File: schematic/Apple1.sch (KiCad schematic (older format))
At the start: 62 parts, among them J1 RCJ-041, J2 USB_A, J4 PWR, J5 ARM_JTAG_SWD, J6 SLOT, J7 EDGE, J8 12V, J9 -12V, SW1 RST, SW2 CLEAR, SW3 PWR, U1 WD65C02, U10 L7805, U2 6821 (W65C21N), U3 ATSAMD21E18A-A, U4 74LS138, U5 AT28C64B-15PU, U6 AS6C62256, U7 74HC00, U9 LD33CV

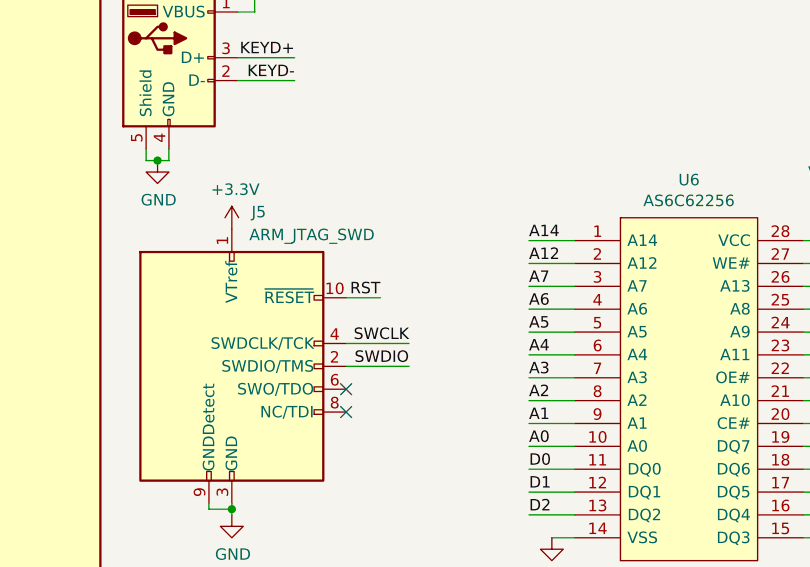
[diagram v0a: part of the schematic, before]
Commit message: final here, attempting to move to compute module to use modern display (HDMI)
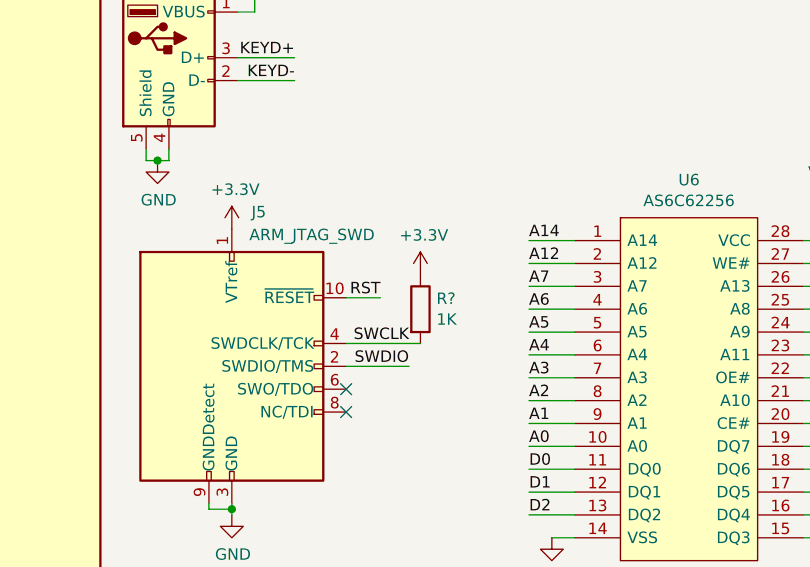
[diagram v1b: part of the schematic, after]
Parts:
- added R?: 1K, symbol Device:R
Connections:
- net +3V3: now also R?.1
- net SWCLK: now also R?.2
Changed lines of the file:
@@
 Text Label 4050 6050 2    50   ~ 0
 SWCLK
-Wire Wire Line
-	4050 6050 3775 6050
 $Comp
 L power:+3.3V #PWR0136
@@
 Wire Wire Line
 	3000 5200 3000 5250
-$Comp
-L Connector:USB_A J2
-U 1 1 5F306103
-P 3000 4800
-F 0 "J2" H 3057 5267 50  0000 C CNN
-F 1 "USB_A" H 3057 5176 50  0000 C CNN
-F 2 "UJ2-AH-4-TH:CUI_UJ2-AH-4-TH" H 3150 4750 50  0001 C CNN
-F 3 " ~" H 3150 4750 50  0001 C CNN
-	1    3000 4800
-	1    0    0    -1
-$EndComp
 Connection ~ 2950 5250
 Wire Wire Line
@@
 Wire Wire Line
 	4650 1025 5375 1025
+$Comp
+L Connector:USB_A J2
+U 1 1 5FAEFE8A
+P 3000 4800
+F 0 "J2" H 3057 5267 50  0000 C CNN
+F 1 "USB_A" H 3057 5176 50  0000 C CNN
+F 2 "UJ2-AH-4-TH:CUI_UJ2-AH-4-TH" H 3150 4750 50  0001 C CNN
+F 3 " ~" H 3150 4750 50  0001 C CNN
+	1    3000 4800
+	1    0    0    -1
+$EndComp
+$Comp
+L Device:R R?
+U 1 1 5FCC40B0
+P 4100 5900
+F 0 "R?" H 4170 5946 50  0000 L CNN
+F 1 "1K" H 4170 5855 50  0000 L CNN
+F 2 "" V 4030 5900 50  0001 C CNN
+F 3 "~" H 4100 5900 50  0001 C CNN
+	1    4100 5900
+	1    0    0    -1
+$EndComp
+Wire Wire Line
+	3775 6050 4100 6050
+$Comp
+L power:+3.3V #PWR?
+U 1 1 5FD027A3
+P 4100 5750
+F 0 "#PWR?" H 4100 5600 50  0001 C CNN
+F 1 "+3.3V" H 4115 5923 50  0000 C CNN
+F 2 "" H 4100 5750 50  0001 C CNN
+F 3 "" H 4100 5750 50  0001 C CNN
+	1    4100 5750
+	1    0    0    -1
+$EndComp
 $EndSCHEMATC

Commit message: rpi final
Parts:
- removed C11: 10uF, Capacitor_THT:CP_Radial_D5.0mm_P2.50mm, symbol Device:CP1_Small
- removed C17: 1uF, Capacitor_THT:CP_Radial_D5.0mm_P2.50mm, symbol Device:C_Small
- removed C8, C9: 0.1uF, Capacitor_THT:C_Rect_L7.0mm_W2.5mm_P5.00mm, symbol Device:C_Small
- removed J1: RCJ-041, CUI_RCJ-041, symbol RCJ-041:RCJ-041
- removed J2: USB_A, UJ2-AH-4-TH:CUI_UJ2-AH-4-TH, symbol Connector:USB_A
- removed J5: ARM_JTAG_SWD, Connector_PinSocket_1.27mm:PinSocket_2x05_P1.27mm_Vertical, symbol Connector:Conn_ARM_JTAG_SWD_10
- removed R10, R11, R12, R13, R14, R25, R6, R7, R8, R9: 1K, Resistor_THT:R_Axial_DIN0207_L6.3mm_D2.5mm_P7.62mm_Horizontal, symbol Device:R_Small
- removed R15, R16, R17, R18, R20, R21, R22, R23, R24: 2k, Resistor_THT:R_Axial_DIN0207_L6.3mm_D2.5mm_P7.62mm_Horizontal, symbol Device:R_Small
- removed R26: 560, Resistor_THT:R_Axial_DIN0207_L6.3mm_D2.5mm_P7.62mm_Horizontal, symbol Device:R_Small
- removed R27: 220, Resistor_THT:R_Axial_DIN0207_L6.3mm_D2.5mm_P7.62mm_Horizontal, symbol Device:R_Small
- removed R5: 3.3K, Resistor_THT:R_Axial_DIN0207_L6.3mm_D2.5mm_P7.62mm_Horizontal, symbol Device:R
- removed R?: 1K, symbol Device:R
- removed SW2: CLEAR, Button_Switch_THT:SW_PUSH_6mm, symbol Switch:SW_SPST
- removed U3: ATSAMD21E18A-A, Package_QFP:TQFP-32_7x7mm_P0.8mm, symbol SAMD:ATSAMD21E18A-A
- removed U9: LD33CV, Package_TO_SOT_THT:TO-220-3_Vertical, symbol Regulator_Linear:LD1117S33TR_SOT223
- added C11, C12, C19, C20: 10uF, Capacitor_SMD:C_0603_1608Metric_Pad1.08x0.95mm_HandSolder, symbol Device:C_Small
- added C2: 0.1uF, Capacitor_SMD:C_0603_1608Metric_Pad1.08x0.95mm_HandSolder, symbol Device:C_Small
- added C21, C22: 0.47uF, Capacitor_SMD:C_0603_1608Metric_Pad1.08x0.95mm_HandSolder, symbol Device:C_Small
- added L1, L2: 4.7uH, Inductor_SMD:L_Bourns-SRN4018, symbol Device:L_Small
- added R19: 100k, Resistor_SMD:R_0603_1608Metric, symbol Device:R_Small
- added U12: AP7315DQ-2.5, Package_TO_SOT_SMD:SOT-23-5, symbol Regulator_Linear:AP7315DQ-25W5-7
- added U5: PAM2306AYPKE, Package_DFN_QFN:WDFN-12-1EP_3x3mm_P0.45mm_EP1.7x2.5mm, symbol Regulator_Switching:PAM2306AYPKE
- C1: renamed from C10; value 10uF -> 0.33uF; footprint Capacitor_THT:CP_Radial_D5.0mm_P2.50mm -> Capacitor_SMD:C_0603_1608Metric_Pad1.08x0.95mm_HandSolder
- C3: renamed from C12; value 1uF -> 0.1uF; footprint Capacitor_THT:CP_Radial_D5.0mm_P2.50mm -> Capacitor_SMD:C_0603_1608Metric_Pad1.08x0.95mm_HandSolder
- renumbered C7 to C10, C1 to C4, C2 to C5, C3 to C6, C4 to C7, C5 to C8, C6 to C9, J4 to J1, J7 to J2, J6 to J3, J8 to J4, J9 to J5, R19 to R5, SW3 to SW1, SW1 to SW2, U4 to U1, U6 to U2, U1 to U3, U7 to U4, U2 to U6, U10 to U7, U5 to U8
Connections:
- net +3V3: now also C20.1, C21.1, L1.2, U12.1 (VIN), U12.3 (EN), U5.4 (FB1)
- net GND: now also C11.2, C12.2, C19.2, C2.1, C20.2, C21.2, C22.2, U12.2 (GND), U5.13 (GND), U5.3 (GND), U5.9 (GND)
- net VCC renamed +5V
- net +5V: now also C11.1, C12.1, R19.1, U5.1 (VIN2), U5.6 (EN1), U5.7 (VIN1)
- new net: C2.2, R19.2, U5.12 (EN2)
- new net: L2.1, U5.2 (LX2)
- new net: L1.1, U5.8 (LX1)
- new net +1V8: C19.1, L2.2, U5.10 (FB2)
- new net +2V5: C22.1, U12.5 (VOUT)
- no-connect marks 10 -> 8
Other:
- moved on the sheet: C1, C3, D1, J1, R1, R2, R3, R4, SW1, SW2, U1, U2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

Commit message: completed schematic
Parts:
- renumbered C4 to C10, C5 to C11, C6 to C12, C7 to C13, C8 to C14, C9 to C15, C10 to C16, C3 to C2, C2 to C3, C11 to C4, C12 to C5, C19 to C6, C20 to C7, C21 to C8, C22 to C9, R19 to R4, R4 to R5, R5 to R6, U3 to U1, U12 to U10, U6 to U2, U2 to U3, U8 to U4, U1 to U5, U5 to U8, U4 to U9

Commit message: finished product v1
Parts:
- removed C3: 0.1uF, Capacitor_SMD:C_0603_1608Metric_Pad1.08x0.95mm_HandSolder, symbol Device:C_Small
- removed C4, C5, C6, C7: 10uF, Capacitor_SMD:C_0603_1608Metric_Pad1.08x0.95mm_HandSolder, symbol Device:C_Small
- removed C8, C9: 0.47uF, Capacitor_SMD:C_0603_1608Metric_Pad1.08x0.95mm_HandSolder, symbol Device:C_Small
- removed L1, L2: 4.7uH, Inductor_SMD:L_Bourns-SRN4018, symbol Device:L_Small
- removed R4: 100k, Resistor_SMD:R_0603_1608Metric, symbol Device:R_Small
- removed U10: AP7315DQ-2.5, Package_TO_SOT_SMD:SOT-23-5, symbol Regulator_Linear:AP7315DQ-25W5-7
- removed U8: PAM2306AYPKE, Package_DFN_QFN:WDFN-12-1EP_3x3mm_P0.45mm_EP1.7x2.5mm, symbol Regulator_Switching:PAM2306AYPKE
- J1: symbol Connector:Barrel_Jack_Switch -> Apple1-rescue:Barrel_Jack_Switch-Connector
- J4, J5: symbol Connector:Conn_01x01_Male -> Apple1-rescue:Conn_01x01_Male-Connector
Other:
- moved on the sheet: D2, R6

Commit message: finished apple 1
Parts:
- C1, C2: footprint Capacitor_SMD:C_0603_1608Metric_Pad1.08x0.95mm_HandSolder -> Capacitor_THT:C_Rect_L7.0mm_W2.5mm_P5.00mm
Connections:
- net GND: no longer J3.MH1, J3.MH2
- no-connect marks 8 -> 10
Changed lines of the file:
@@
 F 0 "C1" H 2325 1025 50  0000 L CNN
 F 1 "0.33uF" H 2300 925 50  0000 L CNN
-F 2 "Capacitor_SMD:C_0603_1608Metric_Pad1.08x0.95mm_HandSolder" H 2250 1000 50  0001 C CNN
+F 2 "Capacitor_THT:C_Rect_L7.0mm_W2.5mm_P5.00mm" H 2250 1000 50  0001 C CNN
 F 3 "~" H 2250 1000 50  0001 C CNN
 	1    2250 1000
@@
 F 0 "C2" H 3000 1025 50  0000 L CNN
 F 1 "0.1uF" H 2975 925 50  0000 L CNN
-F 2 "Capacitor_SMD:C_0603_1608Metric_Pad1.08x0.95mm_HandSolder" H 3250 1000 50  0001 C CNN
+F 2 "Capacitor_THT:C_Rect_L7.0mm_W2.5mm_P5.00mm" H 3250 1000 50  0001 C CNN
 F 3 "~" H 3250 1000 50  0001 C CNN
 	1    3250 1000
@@
 	0    1    1    0
 $EndComp
-$Comp
-L power:GND #PWR034
-U 1 1 5F493605
-P 10300 6200
-F 0 "#PWR034" H 10300 5950 50  0001 C CNN
-F 1 "GND" H 10305 6027 50  0000 C CNN
-F 2 "" H 10300 6200 50  0001 C CNN
-F 3 "" H 10300 6200 50  0001 C CNN
-	1    10300 6200
-	1    0    0    -1
-$EndComp
-Wire Wire Line
-	10300 6200 9375 6200
-Connection ~ 10300 6200
-Wire Wire Line
-	9375 5700 9375 6200
-Wire Wire Line
-	10300 6200 10875 6200
-Wire Wire Line
-	10875 6200 10875 5700
 Wire Wire Line
 	10875 5700 10800 5700
@@
 Wire Wire Line
 	10900 6800 10800 6800
-Wire Wire Line
-	10300 3400 10300 3500
 $Comp
 L AT28C64B-15PU:AT28C64B-15PU U4
@@
 	1    0    0    -1
 $EndComp
-Wire Wire Line
-	10300 3400 10500 3400
-Wire Wire Line
-	10500 3400 10500 3225
-Connection ~ 10500 3225
 Wire Wire Line
 	8950 1525 8950 1625
@@
 	2250 1200 2750 1200
 Connection ~ 2750 1200
+Wire Wire Line
+	9375 6250 10300 6250
+Wire Wire Line
+	9375 5700 9375 6250
+Wire Wire Line
+	10875 5700 10875 6250
+Connection ~ 10300 6250
+Wire Wire Line
+	10300 6250 10875 6250
+$Comp
+L power:GND #PWR?
+U 1 1 6181E987
+P 10300 6250
+F 0 "#PWR?" H 10300 6000 50  0001 C CNN
+F 1 "GND" H 10305 6077 50  0000 C CNN
+F 2 "" H 10300 6250 50  0001 C CNN
+F 3 "" H 10300 6250 50  0001 C CNN
+	1    10300 6250
+	1    0    0    -1
+$EndComp
+NoConn ~ 10300 6200
+NoConn ~ 10300 3500
 $EndSCHEMATC
